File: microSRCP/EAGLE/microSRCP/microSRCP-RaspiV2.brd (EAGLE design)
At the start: 61 x 55.9 mm, 19 parts

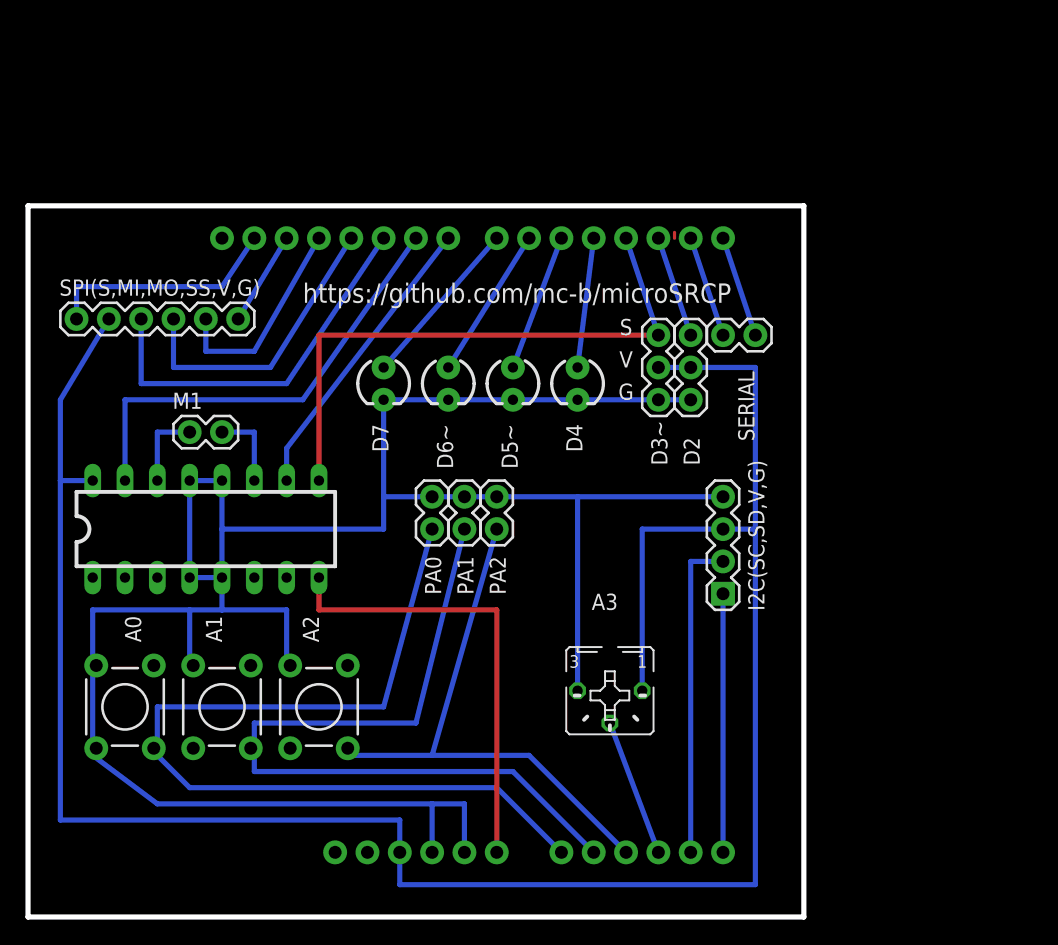
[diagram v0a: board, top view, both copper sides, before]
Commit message: Schaltplaene und Layout von eigenen Shields
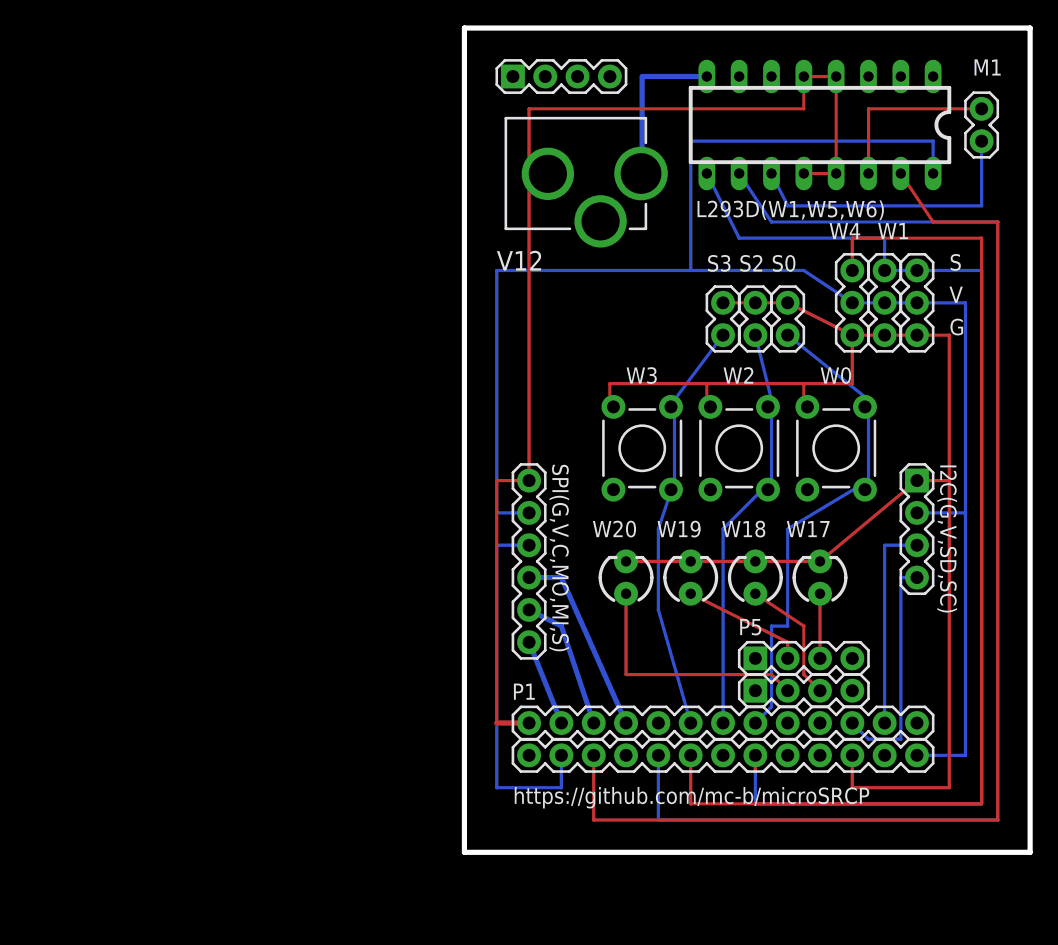
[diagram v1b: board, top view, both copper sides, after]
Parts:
- removed 1: L293D(D3~,D8,D9), SparkFun-AnalogIC:DIL16
- removed 90: (no value), SparkFun-Boards:DUEMILANOVE_SHIELD_NOHOLES_NOLABELS
- removed A0, A1, A2: (no value), SparkFun-Electromechanical:TACTILE-PTH
- removed A3: (no value), pot:B25P
- removed D2, D3~: (no value), SparkFun-Electromechanical:1X03
- removed D4, D5~, D6~, D7: (no value), SparkFun-LED:LED3MM
- removed I2C(SC,SD,V,G): (no value), SparkFun-Connectors:1X04
- removed PA0, PA1, PA2: (no value), SparkFun-Capacitors:1X02
- removed SPI(S,MI,MO,SS,V,G): (no value), SparkFun-Boards:1X06
- added E$1, P1: (no value), SparkFun-Connectors:1X13
- added E$2, E$3, I2C(G,V,SD,SC), P5: (no value), SparkFun-Connectors:1X04
- added L293D(W1,W5,W6): (no value), SparkFun-DigitalIC:DIL16
- added S0, S2: (no value), SparkFun-Capacitors:1X02
- added SPI(G,V,C,MO,MI,S): (no value), SparkFun-Boards:1X06
- added V12: (no value), SparkFun-Connectors:POWER_JACK_PTH_LOCK
- added W0, W2, W3: (no value), SparkFun-Electromechanical:TACTILE-PTH
- added W1, W4: (no value), SparkFun-Capacitors:1X03
- added W17, W18, W19, W20: (no value), SparkFun-LED:LED3MM
- added W1N: (no value), SparkFun-Sensors:1X03
- moved M1 67.2 mm to (74.9, 61.0), turned to 270 degrees
- turned S3 to 90 degrees
- renumbered SERIAL to S3
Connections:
- removed net S$1: 90.D10, SPI(S,MI,MO,SS,V,G).3
- removed net S$10: 90.D2, D2.3
- removed net S$11: 90.D12, SPI(S,MI,MO,SS,V,G).5
- removed net S$12: 90.TX, S3.1
- removed net S$13: 90.RX, S3.2
- removed net S$14: 90.D11, SPI(S,MI,MO,SS,V,G).4
- removed net S$16: 90.A4, I2C(SC,SD,V,G).2
- removed net S$17: 90.A0, PA0.1
- removed net S$18: 90.A1
- removed net S$19: 90.A2, PA2.1
- removed net S$2: 90.A5, I2C(SC,SD,V,G).1
- removed net S$20: PA1.1
- removed net S$21: 90.A3, A3.S
- removed net S$24: 1.14, M1.1
- removed net S$25: 1.10, 90.D8
- removed net S$3: 1.15, 90.D9
- removed net S$4: 90.D13, SPI(S,MI,MO,SS,V,G).6
- removed net S$5: 90.D7, D7.A
- removed net S$6: 90.D6, D6~.A
- removed net S$7: 90.D5, D5~.A
- removed net S$8: 90.D4, D4.A
- removed net S$9: 1.9, 90.D3, D3~.3
- removed net VIN: 1.8, 90.VIN
- new net S0: P1.8, S0.1
- new net S1: E$1.8, L293D(W1,W5,W6).9, W1.3, W1N.3
- new net S17: P5.3, W17.A
- new net S18: E$3.3, W18.A
- new net S19: P5.2, W19.A
- new net S2: P1.7, S2.1
- new net S20: E$3.2, W20.A
- new net S3: P1.6, S3.1
- new net S4: E$1.6, W4.3
- new net S5: E$1.5, L293D(W1,W5,W6).10
- new net S6: E$1.3, L293D(W1,W5,W6).15
- new net SCE0: E$1.2, SPI(G,V,C,MO,MI,S).3
- new net SM1L: L293D(W1,W5,W6).14, M1.1
- new net SM1R: L293D(W1,W5,W6).11, M1.2
- new net SMISO: P1.3, SPI(G,V,C,MO,MI,S).5
- new net SMOSI: P1.4, SPI(G,V,C,MO,MI,S).4
- new net SSCL: I2C(G,V,SD,SC).4, P1.11
- new net SSCLK: P1.2, SPI(G,V,C,MO,MI,S).6
- new net SSDA: I2C(G,V,SD,SC).3, P1.12
- net 5V: now also E$1.13, I2C(G,V,SD,SC).2, L293D(W1,W5,W6).16, SPI(G,V,C,MO,MI,S).2, W1.2, W1N.2, W4.2; no longer 1.16, 90.5V, A3.A, D2.2, D3~.2, I2C(SC,SD,V,G).3, SPI(S,MI,MO,SS,V,G).2
- net GND: now also E$1.11, I2C(G,V,SD,SC).1, S0.2, S2.2, S3.2, W1.1, W17.K, W18.K, W19.K, W1N.1, W20.K, W4.1; no longer 1.12, 1.13, 1.4, 1.5, 90.GND@0, 90.GND@1, A3.E, D2.1, D3~.1, D4.K, D5~.K, D6~.K, D7.K, I2C(SC,SD,V,G).4, PA0.2, PA1.2, PA2.2
- net GND2: now also L293D(W1,W5,W6).12, L293D(W1,W5,W6).13, L293D(W1,W5,W6).4, L293D(W1,W5,W6).5, P1.1, SPI(G,V,C,MO,MI,S).1; no longer 90.GND@2, SPI(S,MI,MO,SS,V,G).1
- net S$22: now also L293D(W1,W5,W6).8; no longer 1.11, M1.2
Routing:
- net S5: track 0.00 -> 101.1 mm
- net S6: track 0.00 -> 93.5 mm
- net S1: track 0.00 -> 92.0 mm
- net S4: track 0.00 -> 83.8 mm
- net GND2: track 18.5 -> 90.2 mm
- net S$17: track 71.0 -> 0.00 mm
- net GND: track 184.2 -> 118.5 mm
- net S$9: track 46.1 -> 0.00 mm
- net S$19: track 43.2 -> 0.00 mm
- net S0: track 0.00 -> 38.9 mm
- net 5V: track 172.5 -> 134.1 mm
- net S$3: track 35.8 -> 0.00 mm
- net VIN: track 35.6 -> 0.00 mm
- net S3: track 0.00 -> 32.3 mm
- net S2: track 0.00 -> 32.2 mm
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- added copper zone on layer 16, net S$1
- removed copper zone on layer 16, net S$15
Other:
- board size 61 x 55.9 mm -> 44.4 x 64.8 mm

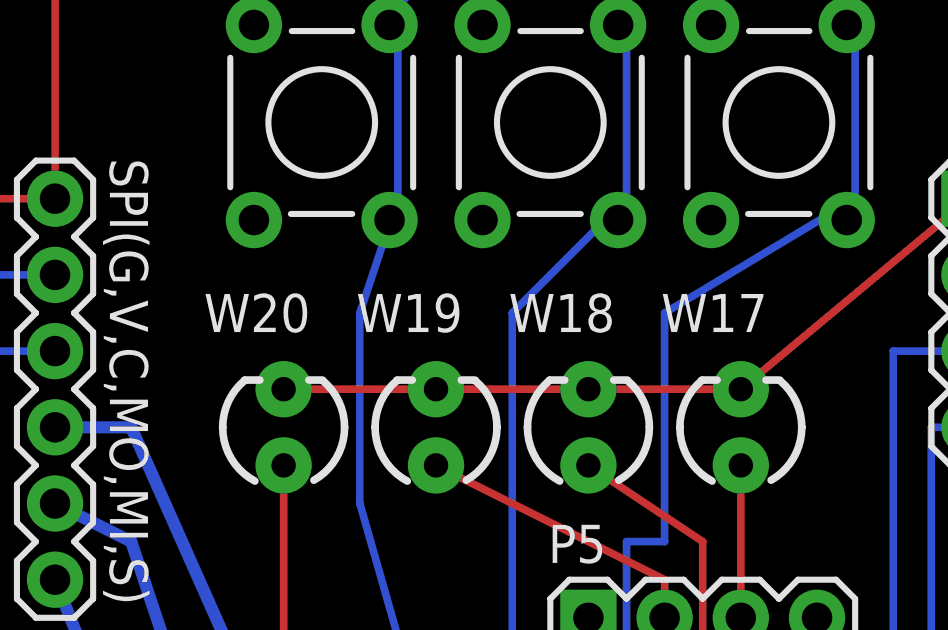
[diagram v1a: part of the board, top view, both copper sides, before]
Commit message: Korrektur Beschriftungen - LED's
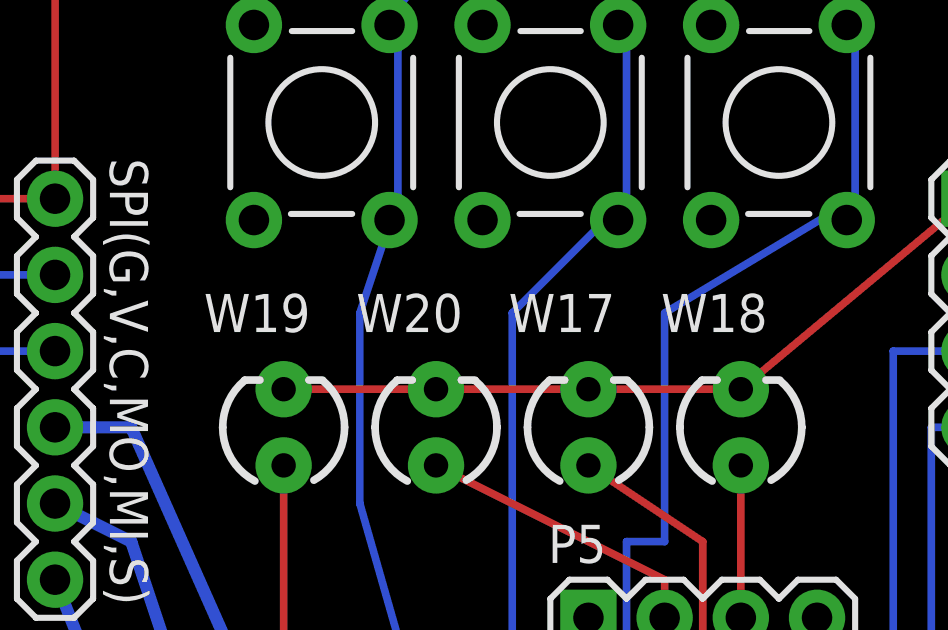
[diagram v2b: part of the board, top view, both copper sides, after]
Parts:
- moved W17 5.08 mm to (57.1, 24.1)
- moved W18 5.08 mm to (62.2, 24.1)
- moved W19 5.08 mm to (47.0, 24.1)
- moved W20 5.08 mm to (52.1, 24.1)
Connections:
- net S17: now also W18.A; no longer W17.A
- net S18: now also W17.A; no longer W18.A
- net S19: now also W20.A; no longer W19.A
- net S20: now also W19.A; no longer W20.A
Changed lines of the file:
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@@
 <attribute name="VALUE" x="69.723" y="60.325" size="1.27" layer="27" ratio="10" rot="R180"/>
 </element>
-<element name="W17" library="SparkFun-LED" package="LED3MM" value="" x="62.23" y="24.13" smashed="yes" rot="R90">
+<element name="W18" library="SparkFun-LED" package="LED3MM" value="" x="62.23" y="24.13" smashed="yes" rot="R90">
 <attribute name="NAME" x="63.119" y="28.575" size="1.27" layer="25" ratio="10" rot="R180"/>
 <attribute name="VALUE" x="63.881" y="26.035" size="1.27" layer="27" ratio="10" rot="R90"/>
 </element>
-<element name="W18" library="SparkFun-LED" package="LED3MM" value="" x="57.15" y="24.13" smashed="yes" rot="R90">
+<element name="W17" library="SparkFun-LED" package="LED3MM" value="" x="57.15" y="24.13" smashed="yes" rot="R90">
 <attribute name="NAME" x="58.039" y="28.575" size="1.27" layer="25" ratio="10" rot="R180"/>
 <attribute name="VALUE" x="58.801" y="26.035" size="1.27" layer="27" ratio="10" rot="R90"/>
 </element>
-<element name="W19" library="SparkFun-LED" package="LED3MM" value="" x="52.07" y="24.13" smashed="yes" rot="R90">
+<element name="W20" library="SparkFun-LED" package="LED3MM" value="" x="52.07" y="24.13" smashed="yes" rot="R90">
 <attribute name="NAME" x="52.959" y="28.575" size="1.27" layer="25" ratio="10" rot="R180"/>
 <attribute name="VALUE" x="53.721" y="26.035" size="1.27" layer="27" ratio="10" rot="R90"/>
 </element>
-<element name="W20" library="SparkFun-LED" package="LED3MM" value="" x="46.99" y="24.13" smashed="yes" rot="R90">
+<element name="W19" library="SparkFun-LED" package="LED3MM" value="" x="46.99" y="24.13" smashed="yes" rot="R90">
 <attribute name="NAME" x="47.879" y="28.575" size="1.27" layer="25" ratio="10" rot="R180"/>
 <attribute name="VALUE" x="48.641" y="26.035" size="1.27" layer="27" ratio="10" rot="R90"/>
@@
 <wire x1="45.72" y1="39.37" x2="45.72" y2="38.1" width="0.254" layer="1"/>
 <wire x1="69.85" y1="31.75" x2="72.39" y2="31.75" width="0.254" layer="1"/>
+<contactref element="W18" pad="K"/>
 <contactref element="W17" pad="K"/>
-<contactref element="W18" pad="K"/>
 <wire x1="57.15" y1="25.4" x2="62.23" y2="25.4" width="0.254" layer="1"/>
+<contactref element="W20" pad="K"/>
+<wire x1="52.07" y1="25.4" x2="57.15" y2="25.4" width="0.254" layer="1"/>
 <contactref element="W19" pad="K"/>
-<wire x1="52.07" y1="25.4" x2="57.15" y2="25.4" width="0.254" layer="1"/>
-<contactref element="W20" pad="K"/>
 <wire x1="46.99" y1="25.4" x2="52.07" y2="25.4" width="0.254" layer="1"/>
 <wire x1="62.23" y1="25.4" x2="69.85" y2="31.75" width="0.254" layer="1"/>
@@
 <signal name="S17">
 <contactref element="P5" pad="3"/>
-<contactref element="W17" pad="A"/>
+<contactref element="W18" pad="A"/>
 <wire x1="62.23" y1="17.78" x2="62.23" y2="22.86" width="0.254" layer="1"/>
 </signal>
@@
 <wire x1="62.23" y1="15.24" x2="60.96" y2="16.51" width="0.254" layer="1"/>
 <wire x1="60.96" y1="16.51" x2="60.96" y2="20.32" width="0.254" layer="1"/>
-<contactref element="W18" pad="A"/>
+<contactref element="W17" pad="A"/>
 <wire x1="60.96" y1="20.32" x2="57.15" y2="22.86" width="0.254" layer="1"/>
 </signal>
@@
 <contactref element="P5" pad="2"/>
 <wire x1="59.69" y1="17.78" x2="59.69" y2="19.05" width="0.254" layer="1"/>
-<contactref element="W19" pad="A"/>
+<contactref element="W20" pad="A"/>
 <wire x1="59.69" y1="19.05" x2="52.07" y2="22.86" width="0.254" layer="1"/>
 </signal>
@@
 <wire x1="59.69" y1="15.24" x2="58.42" y2="16.51" width="0.254" layer="1"/>
 <wire x1="58.42" y1="16.51" x2="46.99" y2="16.51" width="0.254" layer="1"/>
-<contactref element="W20" pad="A"/>
+<contactref element="W19" pad="A"/>
 <wire x1="46.99" y1="16.51" x2="46.99" y2="22.86" width="0.254" layer="1"/>
 </signal>
